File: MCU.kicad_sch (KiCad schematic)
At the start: 12 parts, among them U1 XIAO-ESP32-C3-SMD, U2 SN74LVC1G17DBVR

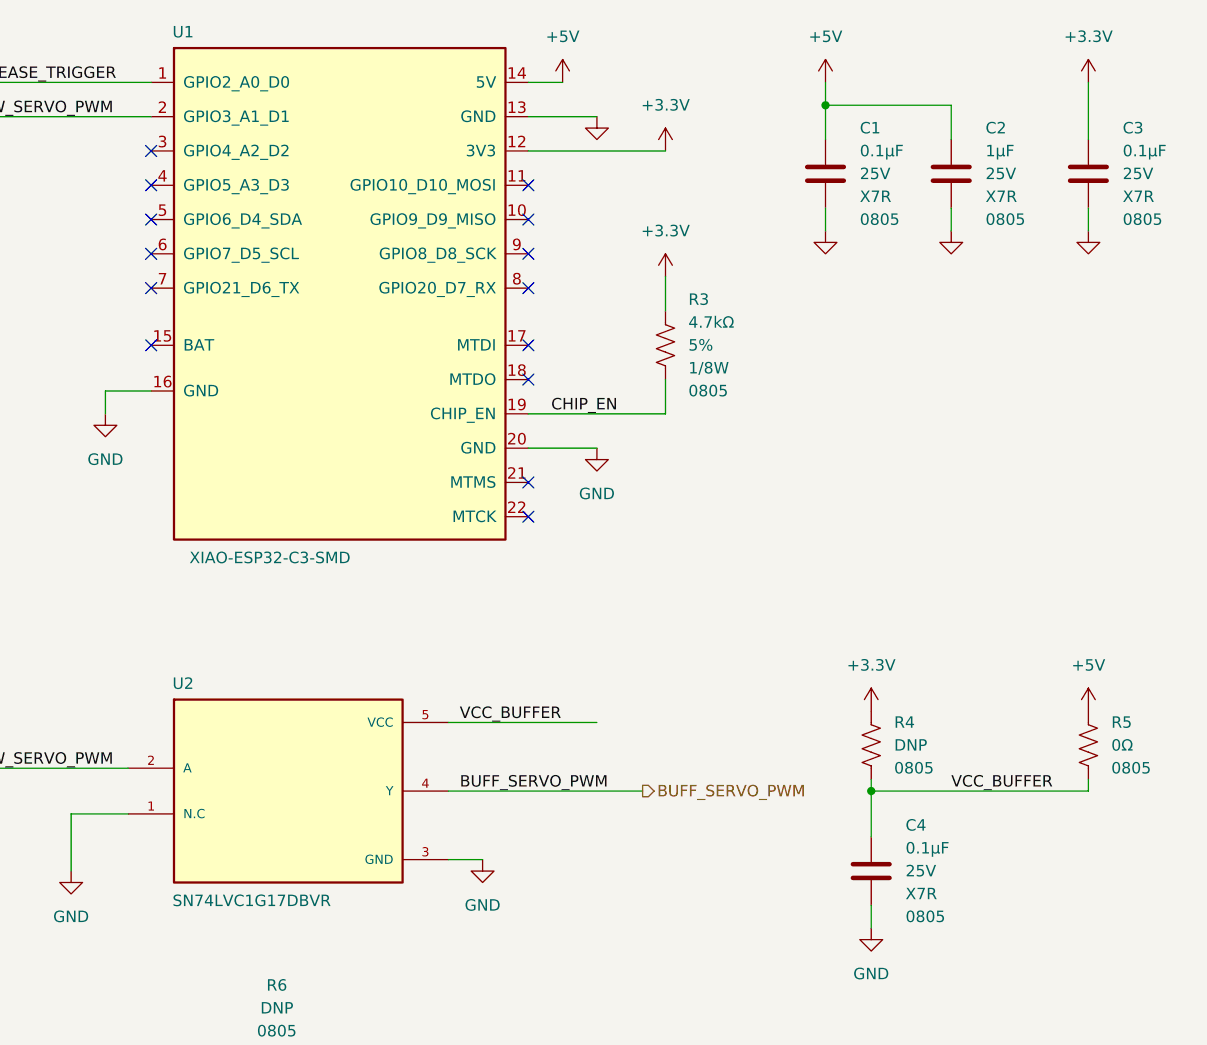
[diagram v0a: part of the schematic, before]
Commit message: drew buck circuit
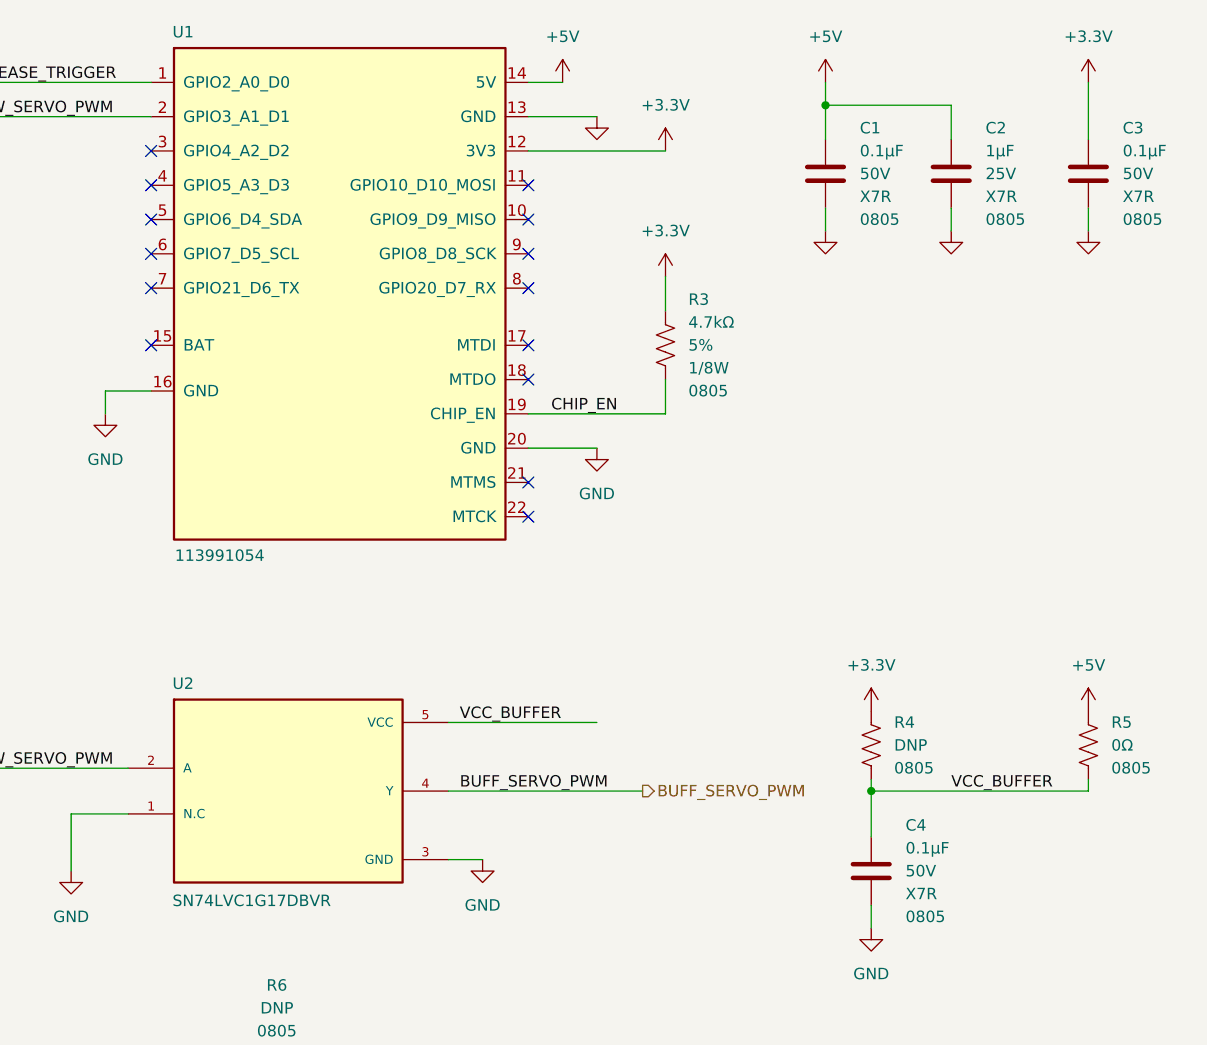
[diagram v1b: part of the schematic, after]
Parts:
- removed C1, C3, C4: CL21B104KACNNNC, Capacitor_SMD:C_0805_2012Metric_Pad1.18x1.45mm_HandSolder, symbol Capacitors_MLCC:CL21B104KACNNNC
- added C1, C3, C4: CL21B104KBCNNNC, Capacitor_SMD:C_0805_2012Metric_Pad1.18x1.45mm_HandSolder, symbol Capacitors_MLCC:CL21B104KBCNNNC
- U1: value XIAO-ESP32-C3-SMD -> 113991054; Other Name (none) -> XIAO-ESP32-C3-SMD
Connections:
- net +3.3V: now also C3.1
- net +5V: now also C1.1
- net GND: now also C1.2, C3.2, C4.2
- net VCC_BUFFER: now also C4.1

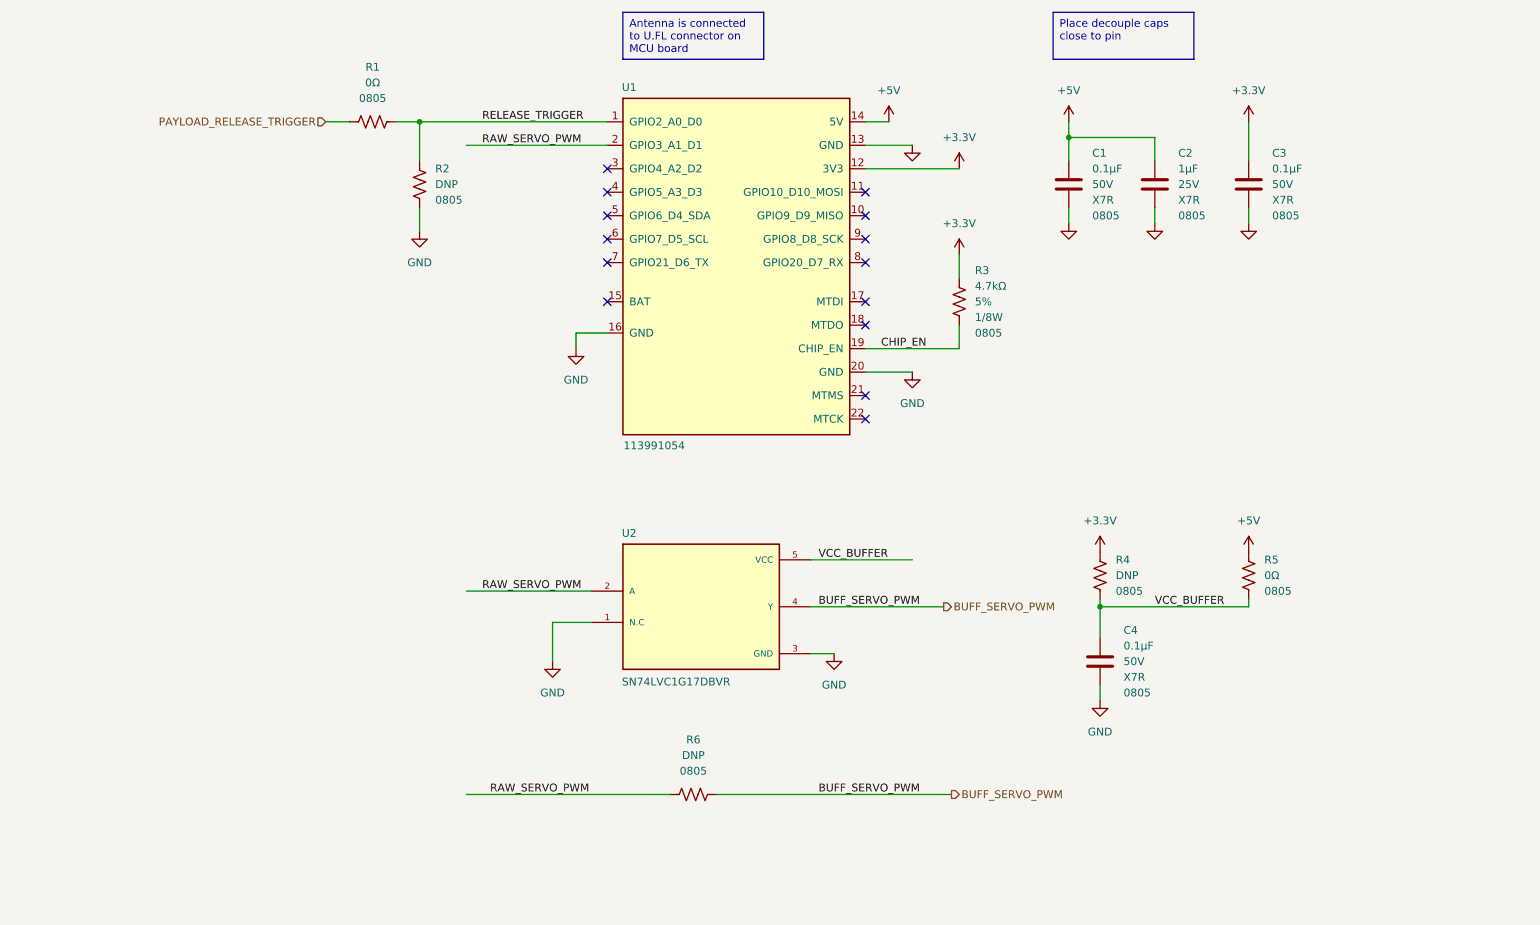
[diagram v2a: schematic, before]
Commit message: Added solenoid driver circuit
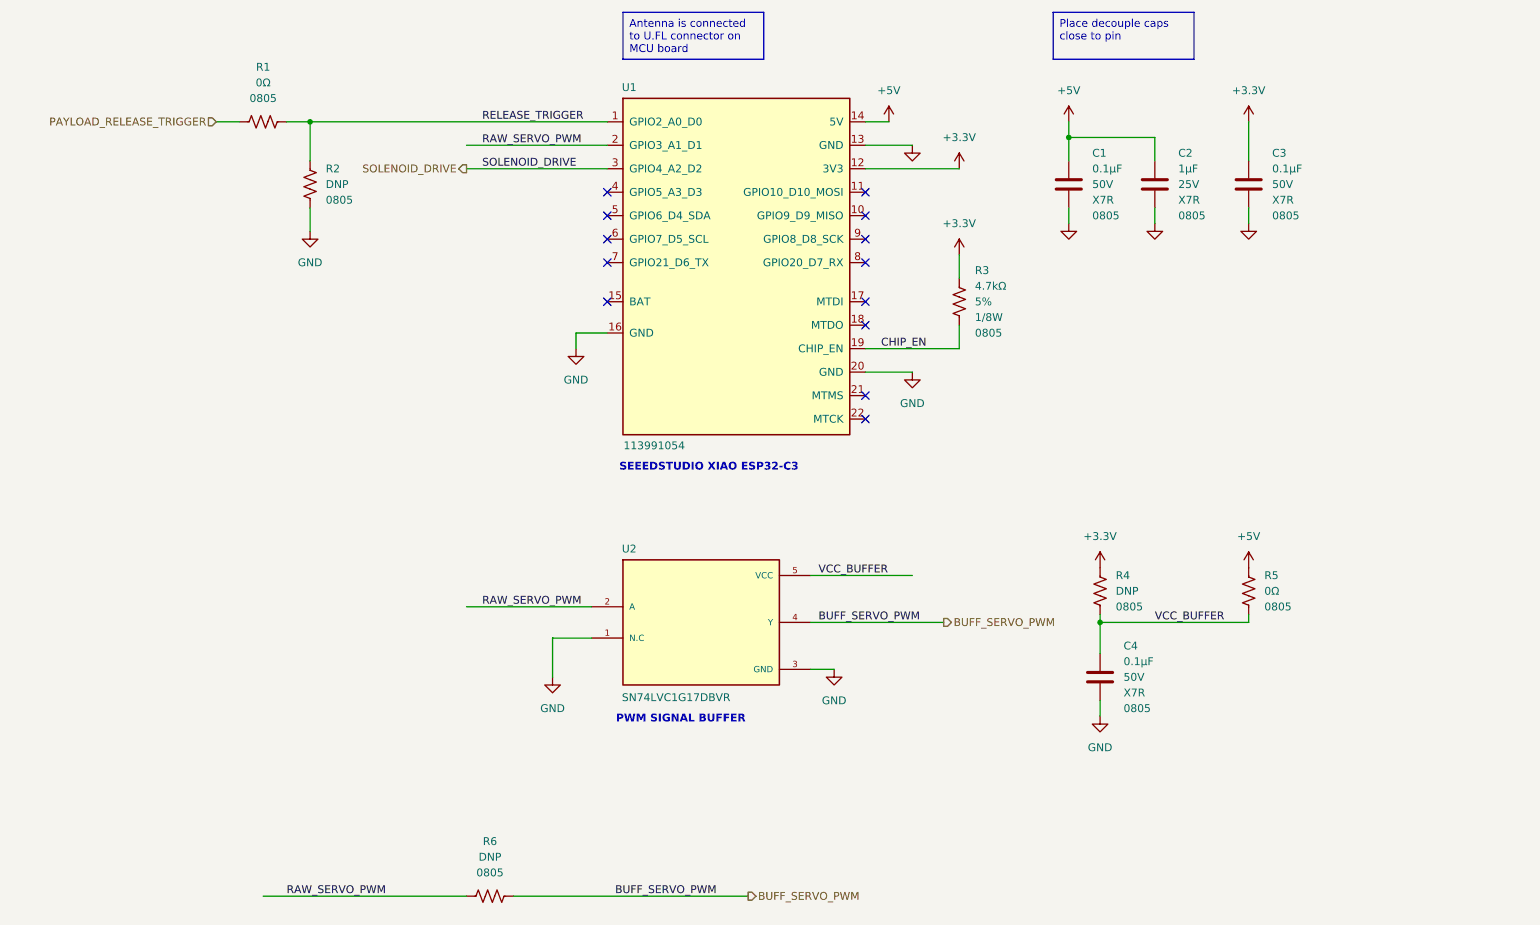
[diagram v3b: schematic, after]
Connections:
- net SOLENOID_DRIVE: now reaches U1.3 (GPIO4_A2_D2)
- no-connect marks 14 -> 13
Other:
- note added: "PWM SIGNAL BUFFER"
- note added: "SEEEDSTUDIO XIAO ESP32-C3"
- moved on the sheet: C4, R1, R2, R4, R5, R6, U2

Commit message: 1st round of rough component placement
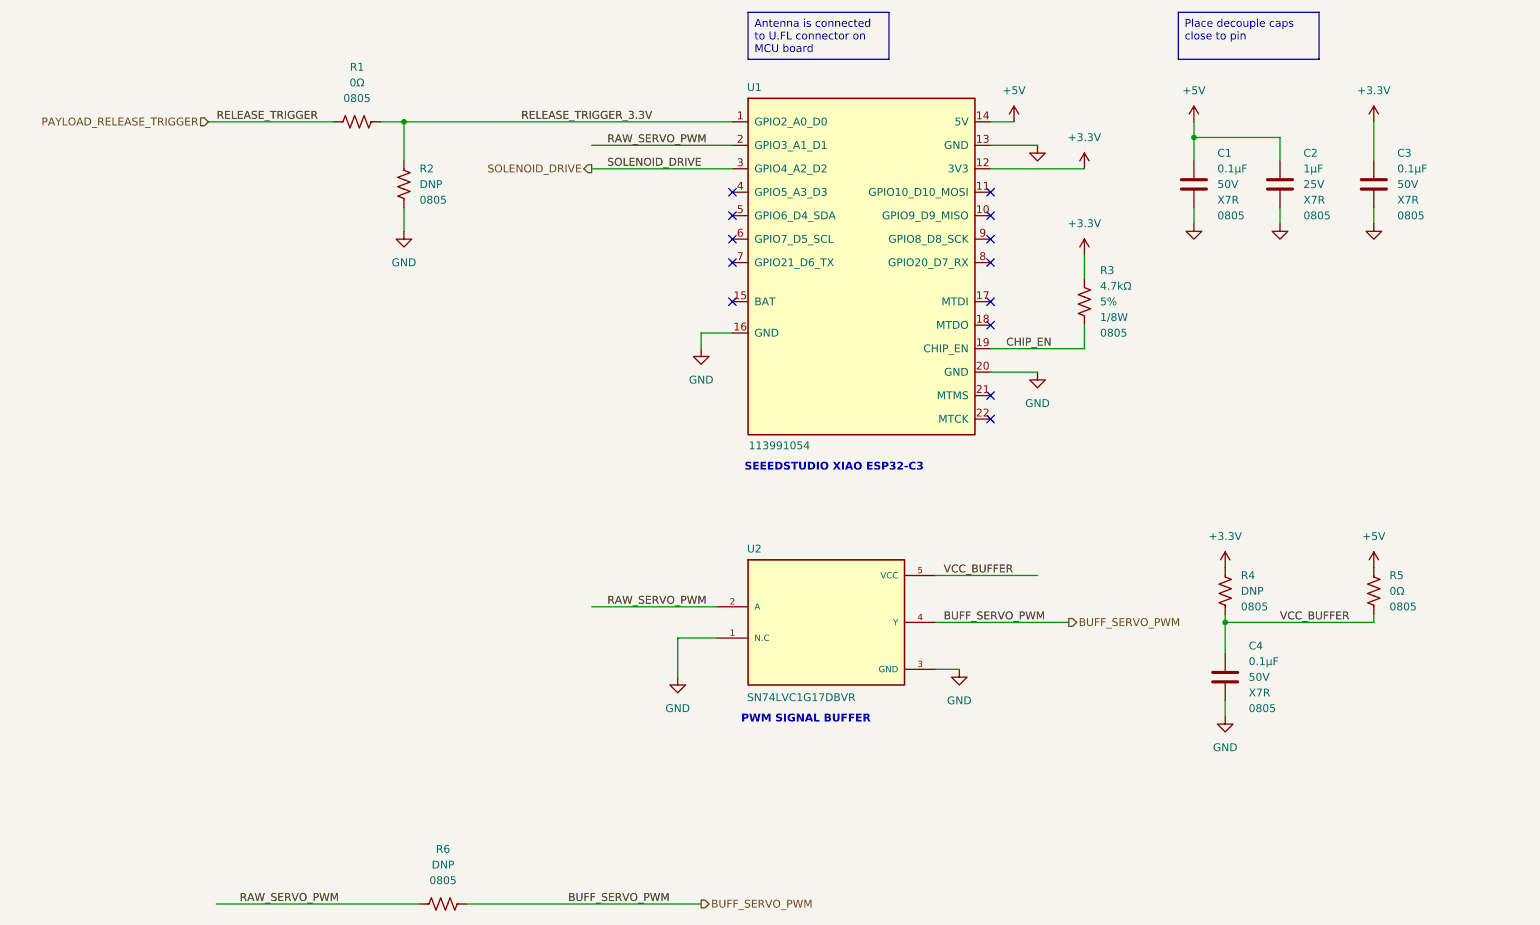
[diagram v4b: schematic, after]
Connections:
- net RELEASE_TRIGGER renamed RELEASE_TRIGGER_3.3V
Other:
- moved on the sheet: C1, C2, C3, C4, R1, R2, R3, R4, R5, R6, U1, U2

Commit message: added i2c + another servo rail
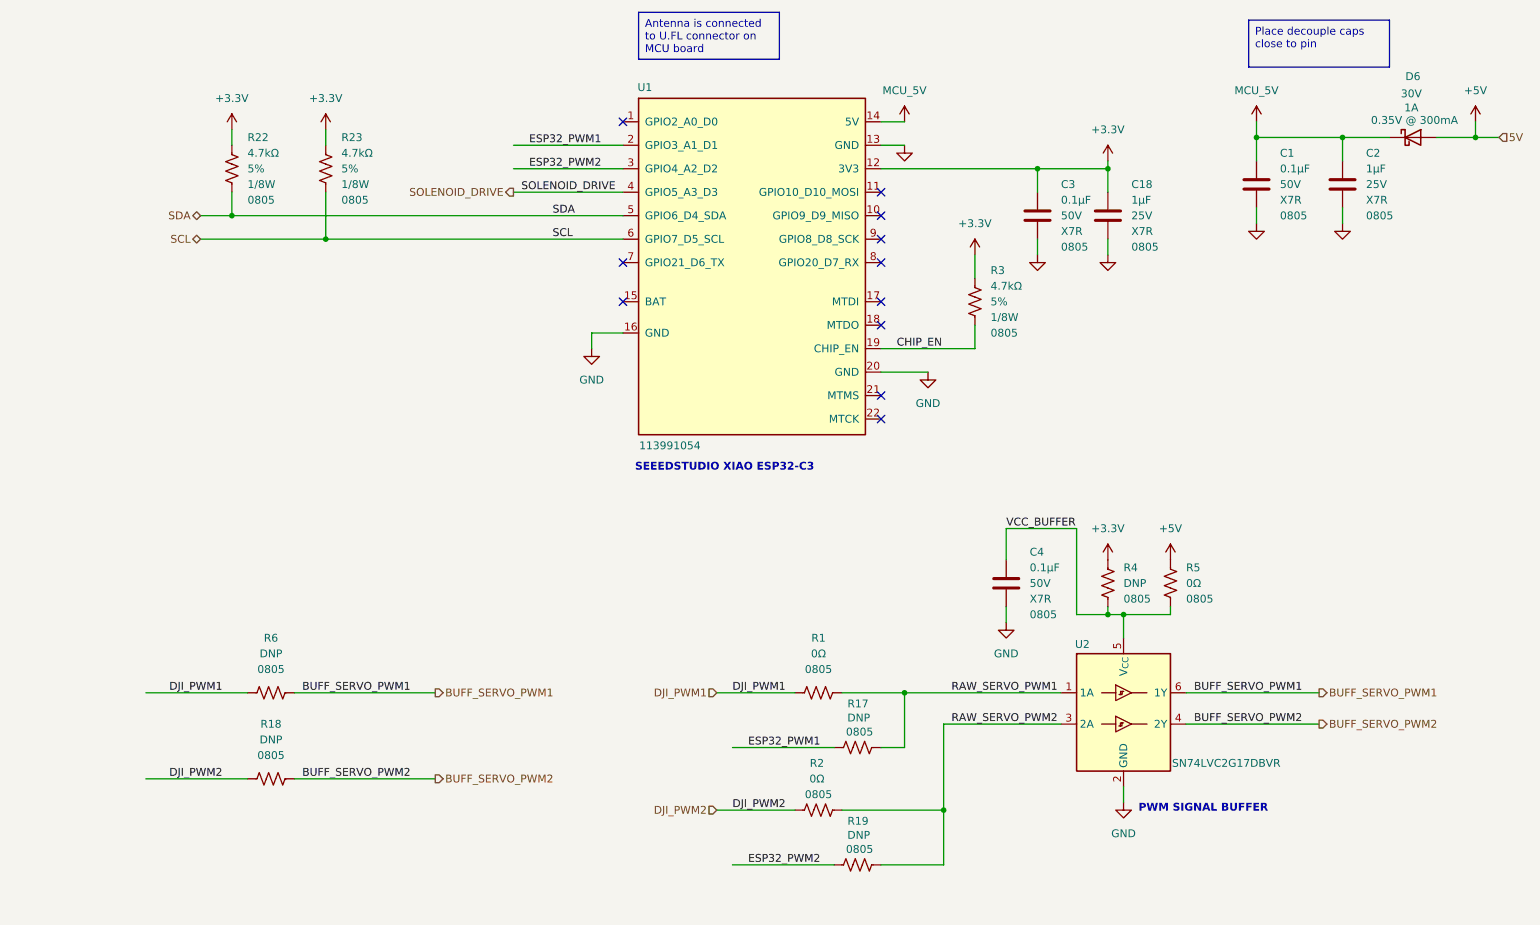
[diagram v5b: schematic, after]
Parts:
- removed R2: DNP 0805, Resistor_SMD:R_0805_2012Metric_Pad1.20x1.40mm_HandSolder, symbol Resistors:DNP_0805
- removed U2: SN74LVC1G17DBVR, Package_TO_SOT_SMD:SOT-23-5_SN74LVC1G17DBVR, symbol Buffer:SN74LVC1G17DBVR
- added C18: CL21B105KAFNNNE, Capacitor_SMD:C_0805_2012Metric_Pad1.18x1.45mm_HandSolder, symbol Capacitors_MLCC:CL21B105KAFNNNE
- added D6: MSS1P3L-M3/89A, Diode_SMD:D_MicroSMP_AK_MSS1P3L-M3_89A, symbol Diode:MSS1P3L-M3/89A
- added R17, R18, R19: DNP 0805, Resistor_SMD:R_0805_2012Metric_Pad1.20x1.40mm_HandSolder, symbol Resistors:DNP_0805
- added R2: RC0805JR-070RL, Resistor_SMD:R_0805_2012Metric_Pad1.20x1.40mm_HandSolder, symbol Resistors:RC0805JR-070RL
- added R22, R23: RMCF0805JT4K70, Resistor_SMD:R_0805_2012Metric_Pad1.20x1.40mm_HandSolder, symbol Resistors:RMCF0805JT4K70
- added U2: SN74LVC2G17DBVR, Package_TO_SOT_SMD:SOT-23-6, symbol 74xGxx:SN74LVC2G17DBVR
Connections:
- net +3.3V: now also C18.1, R22.1, R23.1
- net +5V: now also D6.2 (A); no longer C1.1, C2.1, U1.14 (5V)
- net GND: now also C18.2, U2.2 (GND)
- net SOLENOID_DRIVE: now also U1.4 (GPIO5_A3_D3); no longer U1.3 (GPIO4_A2_D2)
- net VCC_BUFFER: now also U2.5 (V_{CC})
- net SDA: now reaches U1.5 (GPIO6_D4_SDA)
- net SDA: now also R22.2
- net SCL: now reaches U1.6 (GPIO7_D5_SCL)
- net SCL: now also R23.2
- net BUFF_SERVO_PWM renamed BUFF_SERVO_PWM1
- net BUFF_SERVO_PWM1: now also U2.6 (1Y)
- net PAYLOAD_RELEASE_TRIGGER renamed DJI_PWM1
- net DJI_PWM1: now also R6.1
- net RAW_SERVO_PWM renamed ESP32_PWM1
- net ESP32_PWM1: now also R17.1; no longer R6.1
- net RELEASE_TRIGGER_3.3V: no longer names the net of U1.1 (GPIO2_A0_D0)
- net RELEASE_TRIGGER_3.3V: no longer R1.2
- new net BUFF_SERVO_PWM2: R18.2, U2.4 (2Y)
- new net DJI_PWM2: R18.1, R2.1
- new net ESP32_PWM2: R19.1, U1.3 (GPIO4_A2_D2)
- new net MCU_5V: C1.1, C2.1, D6.1 (K), U1.14 (5V)
- new net RAW_SERVO_PWM1: R1.2, R17.2, U2.1 (1A)
- new net RAW_SERVO_PWM2: R19.2, R2.2, U2.3 (2A)
- no-connect marks 13 -> 11
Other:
- moved on the sheet: C1, C2, R3, R4, R5, R6, U1

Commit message: 2nd rev is done
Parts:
- renumbered C18 to C4, C4 to C5, D6 to D1, R22 to R1, R2 to R10, R19 to R11, R23 to R2, R1 to R7, R17 to R8, R18 to R9
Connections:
- net VIN_LED: now reaches U1.7 (GPIO21_D6_TX)
- no-connect marks 11 -> 10
